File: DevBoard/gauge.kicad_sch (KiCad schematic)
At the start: 79 parts, among them J101 Pack (welded 4S) - use instea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, J102 Cell 1 NTC 10k 103AT, J103 EV2400 SMBus, J104 Bench PACK_P, J105 Cell 2 NTC 10k 103AT, J106 Cell 3 NTC 10k 103AT, J107 Cell 4 NTC 10k 103AT, Q101 AGM404AP1, Q102 AGM404AP1, Q103 AO3400A, Q104 AO3400A, SW101 WAKE, U101 BQ40Z50RSMR-R2, U102 BQ294700DSGR

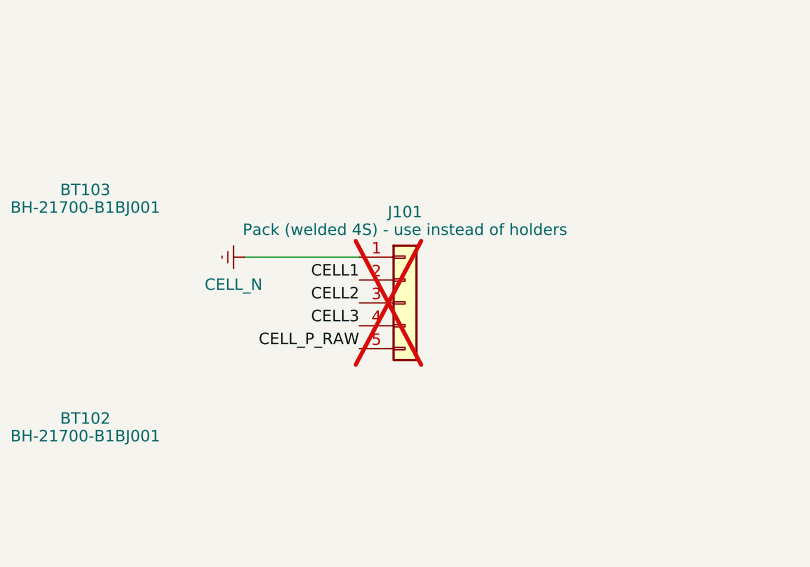
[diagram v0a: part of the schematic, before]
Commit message: Dev board: 10R gate resistors with turn-off diodes; remove TMP1075 sensors
Gate drive (both ports): R444-R447 / R544-R547 0R -> 10R, with a BAT54WS
(D406-D409 / D506-D509) across each, cathode at the BQ25756 driver pin, so
turn-off bypasses the resistor and the 45 ns dead time is kept. Notes on the
gate resistors rewritten (they named the wrong drivers). Diodes are staged
below the board for hand placement.

Board temperature (rev A8): U302-U306 and C308-C312 removed. Temperatures
now come from the gauge (DAStatus2: TS1-TS4, cell, FET, die; readable
sealed) and from each BQ25756 TS NTC via the TPS25751 'I2Cr' pass-through
(REG0x37 TS_ADC). IRQ_N now has three sources. Docs, power budget and
scripts updated.

Also includes the author's own uncommitted schematic and README edits.
ERC: 8 known warnings; DRC schematic parity: 0 footprint errors.

Co-Authored-By: Claude Opus 5.5 <noreply@anthropic.com>
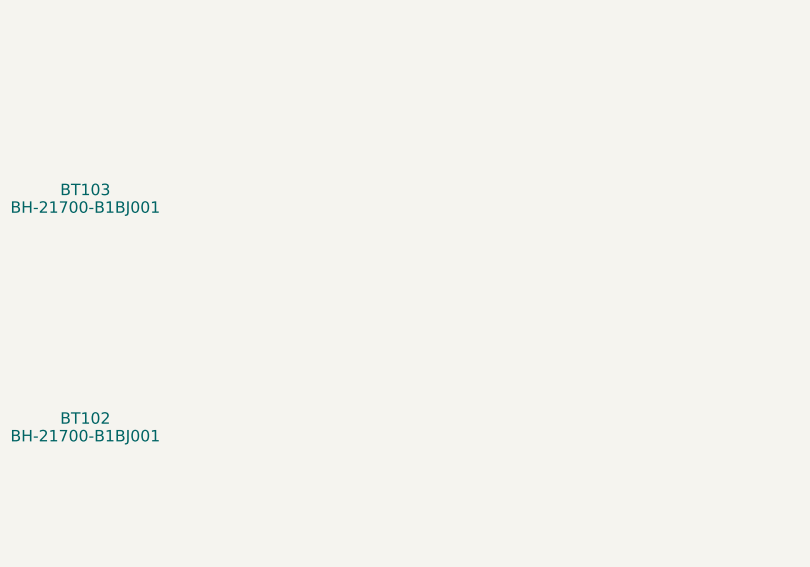
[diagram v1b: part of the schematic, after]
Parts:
- removed J101: Pack (welded 4S) - use instead of holders, TerminalBlock_Phoenix:TerminalBlock_Phoenix_MKDS-1,5-5-5.08_1x05_P5.08mm_Horizontal, symbol Connector_Generic:Conn_01x05
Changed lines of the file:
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@@
 	(wire
 		(pts
-			(xy 81.28 93.98) (xy 68.58 93.98)
-		)
-		(stroke
-			(width 0)
-			(type default)
-		)
-	)
-	(wire
-		(pts
 			(xy 321.31 96.52) (xy 325.12 96.52)
 		)
@@
 		)
 	)
-	(label "CELL2"
-		(at 81.28 99.06 180)
-		(effects
-			(font
-				(size 1.27 1.27)
-			)
-			(justify right bottom)
-		)
-	)
 	(label "CELL_P_RAW"
 		(at 270.51 96.52 180)
@@
 		)
 	)
-	(label "CELL1"
-		(at 81.28 96.52 180)
-		(effects
-			(font
-				(size 1.27 1.27)
-			)
-			(justify right bottom)
-		)
-	)
 	(label "CELL3"
 		(at 38.1 83.82 90)
@@
 		)
 	)
-	(label "CELL3"
-		(at 81.28 101.6 180)
-		(effects
-			(font
-				(size 1.27 1.27)
-			)
-			(justify right bottom)
-		)
-	)
 	(label "DSG"
 		(at 228.6 138.43 0)
@@
 		)
 	)
-	(label "CELL_P_RAW"
-		(at 81.28 104.14 180)
-		(effects
-			(font
-				(size 1.27 1.27)
-			)
-			(justify right bottom)
-		)
-	)
 	(label "CELL_P"
 		(at 384.81 99.06 0)
@@
 	)
 	(symbol
-		(lib_id "Connector_Generic:Conn_01x05")
-		(at 86.36 99.06 0)
-		(unit 1)
-		(body_style 1)
-		(exclude_from_sim no)
-		(in_bom yes)
-		(on_board yes)
-		(in_pos_files yes)
-		(dnp yes)
-		(property "Reference" "J101"
-			(at 86.36 88.96 0)
-			(show_name no)
-			(do_not_autoplace no)
-			(effects
-				(font
-					(size 1.27 1.27)
-				)
-			)
-		)
-		(property "Value" "Pack (welded 4S) - use instead of holders"
-			(at 86.36 90.93 0)
-			(show_name no)
-			(do_not_autoplace no)
-			(effects
-				(font
-					(size 1.27 1.27)
-				)
-			)
-		)
-		(property "Footprint" "TerminalBlock_Phoenix:TerminalBlock_Phoenix_MKDS-1,5-5-5.08_1x05_P5.08mm_Horizontal"
-			(at 86.36 99.06 0)
-			(hide yes)
-			(show_name no)
-			(do_not_autoplace no)
-			(effects
-				(font
-					(size 1.27 1.27)
-				)
-			)
-		)
-		(property "Datasheet" ""
-			(at 86.36 99.06 0)
-			(hide yes)
-			(show_name no)
-			(do_not_autoplace no)
-			(effects
-				(font
-					(size 1.27 1.27)
-				)
-			)
-		)
-		(property "Description" "Generic connector, single row, 01x05, script generated (kicad-library-utils/schlib/autogen/connector/)"
-			(at 86.36 99.06 0)
-			(hide yes)
-			(show_name no)
-			(do_not_autoplace no)
-			(effects
-				(font
-					(size 1.27 1.27)
-				)
-			)
-		)
-		(property "Notes" "Fit only when the welded pack is used, and never with cells in the holders"
-			(at 86.36 99.06 0)
-			(hide yes)
-			(show_name no)
-			(do_not_autoplace no)
-			(effects
-				(font
-					(size 1.27 1.27)
-				)
-			)
-		)
-		(pin "1"
-		)
-		(pin "2"
-		)
-		(pin "3"
-		)
-		(pin "4"
-		)
-		(pin "5"
-		)
-		(instances
-			(project "MonolithDev"
-				(path "/f83241ae-2bb3-4ed7-b986-c0a03971de0a/5f8e2264-136e-4c01-877f-88ca3aa05650"
-					(reference "J101")
-					(unit 1)
-				)
-			)
-		)
-	)
-	(symbol
 		(lib_id "power:VCC")
 		(at 189.23 33.02 270)
@@
 					(unit 1)
 				)
-			)
-		)
-	)
-	(symbol
-		(lib_id "power:GNDREF")
-		(at 68.58 93.98 270)
-		(unit 1)
-		(body_style 1)
-		(exclude_from_sim no)
-		(in_bom yes)
-		(on_board yes)
-		(in_pos_files yes)
-		(dnp no)
-		(property "Reference" "#PWR109"
-			(at 68.58 93.98 0)
-			(hide yes)
-			(show_name no)
-			(do_not_autoplace no)
-			(effects
-				(font
-					(size 1.27 1.27)
-				)
-			)
-		)
-		(property "Value" "CELL_N"
-			(at 67.31 97.03 90)
-			(show_name no)
-			(do_not_autoplace no)
-			(effects
-				(font
-					(size 1.27 1.27)
-				)
-			)
-		)
-		(property "Footprint" ""
-			(at 68.58 93.98 0)
-			(hide yes)
-			(show_name no)
-			(do_not_autoplace no)
-			(effects
-				(font
-					(size 1.27 1.27)
-				)
-			)
-		)
-		(property "Datasheet" ""
-			(at 68.58 93.98 0)
-			(hide yes)
-			(show_name no)
-			(do_not_autoplace no)
-			(effects
-				(font
-					(size 1.27 1.27)
-				)
-			)
-		)
-		(property "Description" "Power symbol creates a global label with name \"GNDREF\" , reference supply ground"
-			(at 68.58 93.98 0)
-			(hide yes)
-			(show_name no)
-			(do_not_autoplace no)
-			(effects
-				(font
-					(size 1.27 1.27)
-				)
-			)
-		)
-		(pin "1"
-		)
-		(instances
-			(project "MonolithDev"
-				(path "/f83241ae-2bb3-4ed7-b986-c0a03971de0a/5f8e2264-136e-4c01-877f-88ca3aa05650"
-					(reference "#PWR109")
-					(unit 1)
-				)
